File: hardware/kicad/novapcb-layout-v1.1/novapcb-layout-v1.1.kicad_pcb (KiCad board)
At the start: 6 copper layers, 90 x 70 mm, 129 parts, among them J1 USB-C_2.0, J10 CRSF_solder_pad, J11 ESC_solder_pad, J12 ESC_solder_pad, J13 ESC_solder_pad, J14 ESC_solder_pad, J15 ESC_solder_pad, J16 ESC_solder_pad, J17 ESC_solder_pad, J18 ESC_solder_pad, J19 MAUCH2_6P, J2 microSD_DM3AT, J20 CAN_4P, J3 TELEM_6P, J4 MAUCH_6P, J5 GPS_MAG_10P, J9 SWD_10P, Q2 AO3401A, Q3 AO4262E, Q4 AO4262E, Q5 AO3400A, U1 STM32H743VITx, U11 LM74700-Q1, U12 LM74700-Q1, U13 LP5907MFX-3.3, U14 TJA1051TK/3, U15 PESD2CAN, U2 AP2112K-3.3, U3 ICM-42688-P_LGA-14_2.5x3mm_P0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, U4 DPS310, U5 USBLC6-2P6, U6 TPS25940A, U7 LPS22HB, U8 BMI088, U9 LSM6DSV16X, Y1 8MHz

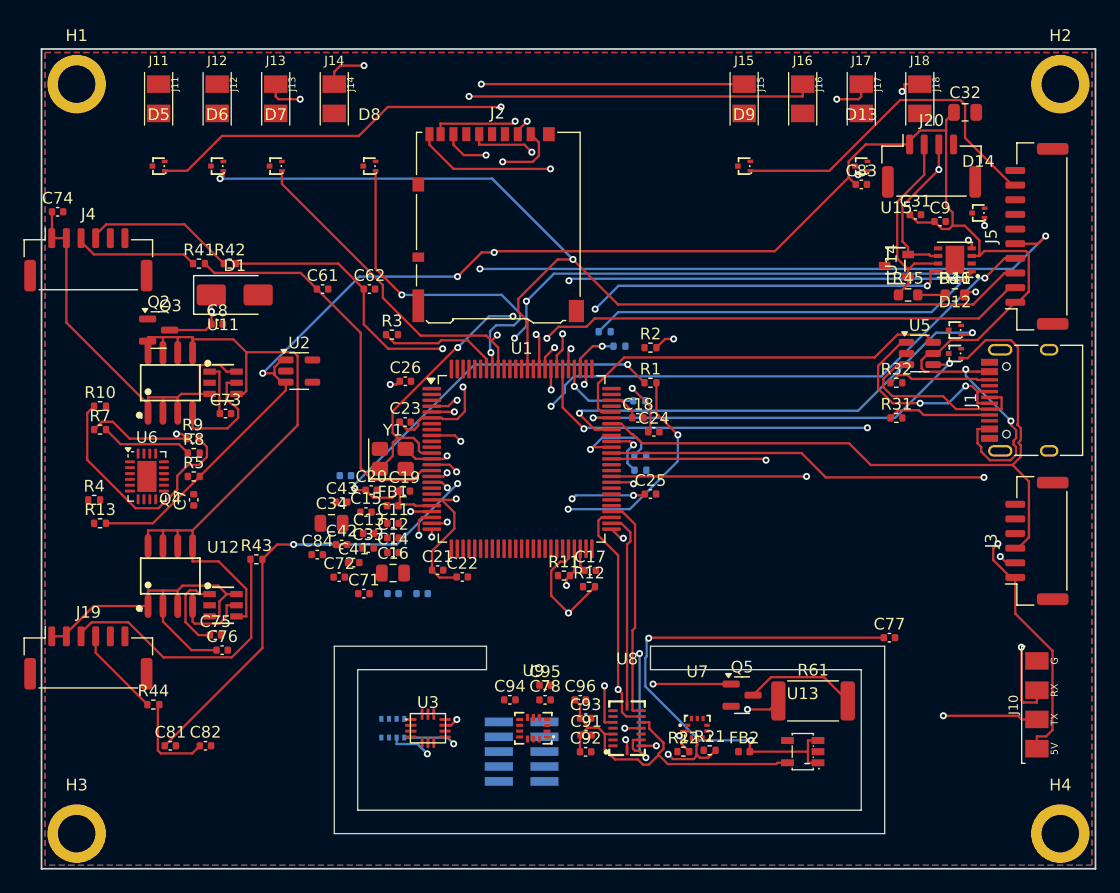
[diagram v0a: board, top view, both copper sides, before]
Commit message: hw: R4 pivot to 4-signal stackup (master 2026-05-22 Option A)
After Option B (A* finishing pass) stalled on plane-via interaction
modeling, master directed Option A: 4 signal layers + full Freerouting.

NEW stackup (same JLC 6-layer fab — only roles change):
  L1 Sig / L2 GND / L3 SIGNAL / L4 SIGNAL / L5 GND / L6 Sig
- 4 signal layers (was 3) — more routing room
- 2 GND planes (L2/L5) preserved for return path / impedance reference
- L3 +3V3 plane removed → L3 becomes signal
- +5V poured on L1 (W block X=2..30, Y=14..56) for 3A current
- +3V3 poured on L6 (MCU+sensors region X=20..80, Y=15..55) for short
  via stitches to consumers

Mitigation per master: L3/L4 are adjacent signal layers (no plane
between). Sensitive nets (3 IMU SPI buses + USB pair) to stay on
outer layers L1/L6 (well-referenced to L2/L5 GND). Bulk to L3/L4.

USB impedance unchanged: L1/L6 still ref L2/L5 GND at h=0.21mm
(prepreg 7628) → W=0.30/S=0.10 → Z_diff=94.4Ω ✓

PCB stripped (988 tracks/113 vias removed). Freerouting -mp 30 now
running with 4h safety-net timeout (will let natural completion +
SES verify, never guillotine).

Co-Authored-By: Claude Opus 4.7 <noreply@anthropic.com>
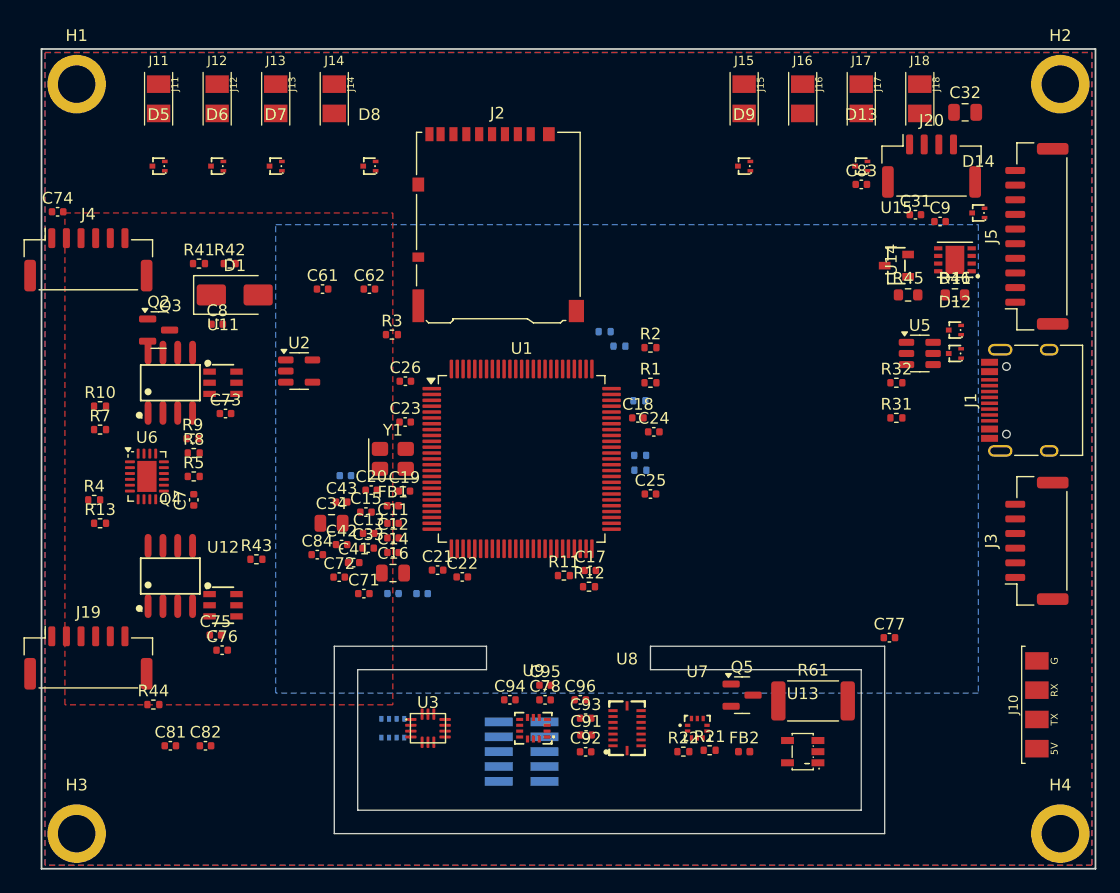
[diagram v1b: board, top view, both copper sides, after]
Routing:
- net +5V: track 243.0 -> 0.00 mm, vias 7 -> 0
- net I2C1_SDA: track 135.8 -> 0.00 mm, vias 5 -> 0
- net I2C1_SCL: track 117.9 -> 0.00 mm, vias 4 -> 0
- net SDMMC1_CMD: track 99.2 -> 0.00 mm, vias 4 -> 0
- net GPS1_TX: track 94.1 -> 0.00 mm, vias 2 -> 0
- net GPS1_RX: track 86.7 -> 0.00 mm, vias 2 -> 0
- net USART6_RX: track 84.9 -> 0.00 mm, vias 3 -> 0
- net USART6_TX: track 78.6 -> 0.00 mm, vias 3 -> 0
- net IMU2_GYR_CS: track 76.7 -> 0.00 mm, vias 2 -> 0
- net MOT6: track 69.3 -> 0.00 mm, vias 2 -> 0
- net VBAT: track 64.5 -> 0.00 mm, vias 2 -> 0
- net MOT5: track 63.3 -> 0.00 mm, vias 2 -> 0
- net USART1_TX: track 62.4 -> 0.00 mm, vias 3 -> 0
- net +5V_BEC: track 61.7 -> 0.00 mm
- net USART1_RX: track 60.4 -> 0.00 mm
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- added copper zone on B.Cu, net +3V3
- added copper zone on F.Cu, net +5V
- removed copper zone on In2.Cu, net +3V3

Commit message: hw: R4 A* + via-cleanup post-processor — 500+ → 33 DRC
Per master 2026-05-22: A* topological + path-level via cleanup.

Key insight master's directive captured: A* finds 14/14 topological
routes. The ONLY problem was via quality (consecutive layer-flip
artifacts). FIX the vias, keep the paths.

Post-processor steps:
1. A* finds path on 3-signal stackup (L1/L4/L6).
2. PATH-LEVEL collapse: walk path; any layer excursion ≤10 cells with
   no useful routing between → DELETE the via pair, keep on origin
   layer. Eliminates zigzag artifacts.
3. Standard corner-collapse.
4. Apply tracks + snapped vias to PCB.
5. Refill plane zones (auto-voids antipads around real vias).

Result: **33 DRC (was 500+ before cleanup)**.
- 14/14 nets routed topologically
- 14 shorts (specific via-on-track conflicts on L4 — 7 net pairs)
- 6 copper_edge_clearance
- 143 unconnected items (the 14 new routes may have endpoint gaps;
  was 112 before — net regression of 31 unconnected)

PCB: 1143 tracks + 147 vias (was 988/113).
Total runtime: 42 seconds.

The 14 shorts are SPECIFIC conflicts (master's "small set" for
vision-loop). Locations + nets logged. Standing by per master:
"If a meaningful DRC residual genuinely remains — STOP and report
exactly which spots; vision-loop those."

Co-Authored-By: Claude Opus 4.7 <noreply@anthropic.com>
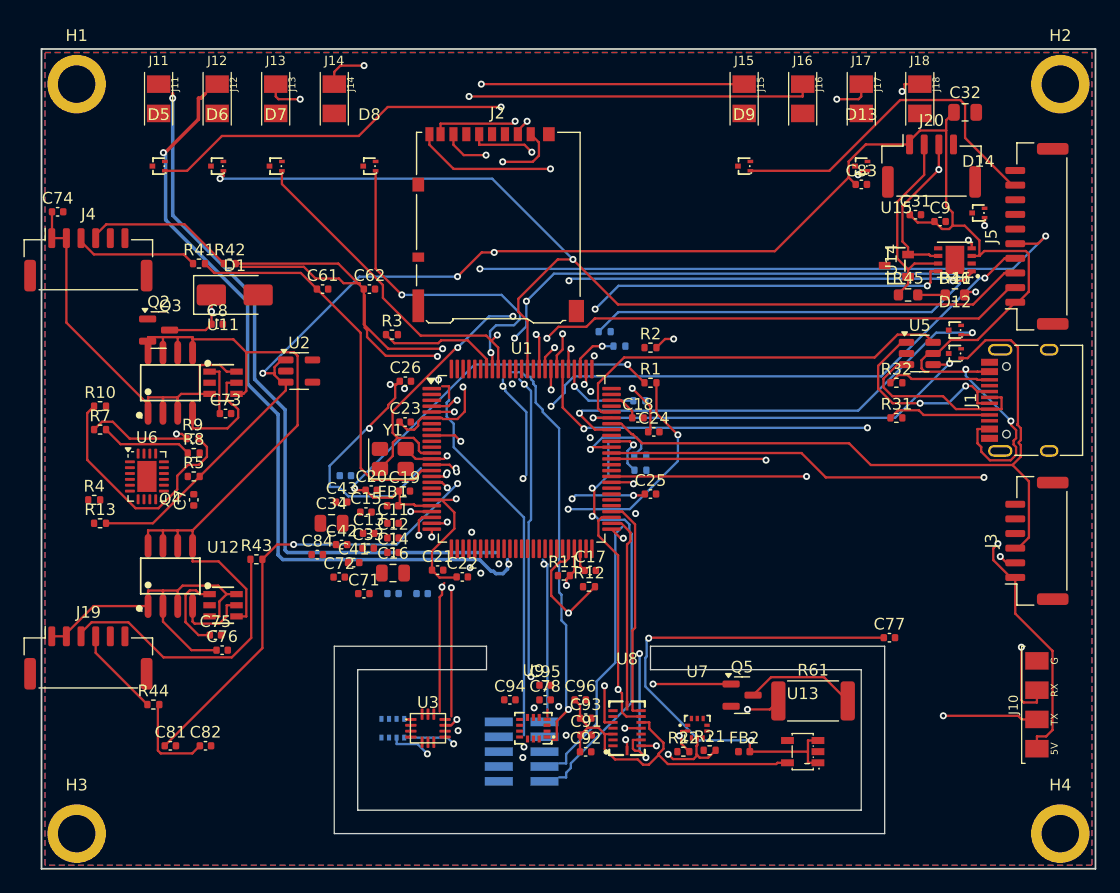
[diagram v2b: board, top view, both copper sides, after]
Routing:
- net +5V: track 0.00 -> 243.0 mm, vias 0 -> 7
- net I2C1_SDA: track 0.00 -> 135.8 mm, vias 0 -> 5
- net I2C1_SCL: track 0.00 -> 117.9 mm, vias 0 -> 4
- net SDMMC1_CMD: track 0.00 -> 99.2 mm, vias 0 -> 4
- net GPS1_TX: track 0.00 -> 94.1 mm, vias 0 -> 2
- net NRST: track 0.00 -> 91.6 mm, vias 0 -> 6
- net GPS1_RX: track 0.00 -> 86.7 mm, vias 0 -> 2
- net USART6_RX: track 0.00 -> 84.9 mm, vias 0 -> 3
- net USART6_TX: track 0.00 -> 78.6 mm, vias 0 -> 3
- net IMU2_GYR_CS: track 0.00 -> 76.7 mm, vias 0 -> 2
- net MOT6: track 0.00 -> 69.3 mm, vias 0 -> 2
- net BATT_CURRENT_SENS: track 0.00 -> 66.2 mm, vias 0 -> 4
- net MOT2: track 0.00 -> 66.1 mm, vias 0 -> 2
- net VBAT: track 0.00 -> 64.5 mm, vias 0 -> 2
- net MOT5: track 0.00 -> 63.3 mm, vias 0 -> 2
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- added copper zone on In2.Cu, net +3V3
- removed copper zone on B.Cu, net +3V3
- removed copper zone on F.Cu, net +5V

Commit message: hw: R4 step 1 connectivity — 143→57 unconnected (master 2026-05-22)
Two fixes applied to A* + via-cleanup state:
1. fix_endpoints.py: added 9 extending segments to close A*-route
   endpoint gaps (cell-grid vs pad-center mismatch). 143 → 137.
2. run_stitch_plane_nets.py: 170 +3V3/GND stitch vias placed (the
   plane stitching was never run after Freerouting 88.8% state).
   137 → 57.

Total connectivity progress: 143 → 57 unconnected (-86) — close to
master's target ~8.

DRC went 33 → 73 because stitch introduced new clashes:
- 21 stitch attempts FAILED (no clear via spot) — those +3V3/GND
  pads still unconnected
- 7 tracks_crossing (stitches on top of A* tracks)
- Plus 14 AVC shorts still present

Remaining 57 unconnected breakdown (top nets):
  GND (10), SWCLK (3), SPI3_SCK (3), USBC_CC2 (2), SPI3_MOSI (2),
  SPI1_MOSI (2), SPI1_MISO (2), NRST (2), IMU3_CS (2), BUZZER (2)
Plus several +3V3 MCU pins (11, 27, 50, 75, 100) and +3V3_IMU pads
(from the 21 stitch failures).

Per master step 1 → step 2: now address the 14 specific via-on-track
shorts (the master's small-set vision-loop targets).

Co-Authored-By: Claude Opus 4.7 <noreply@anthropic.com>
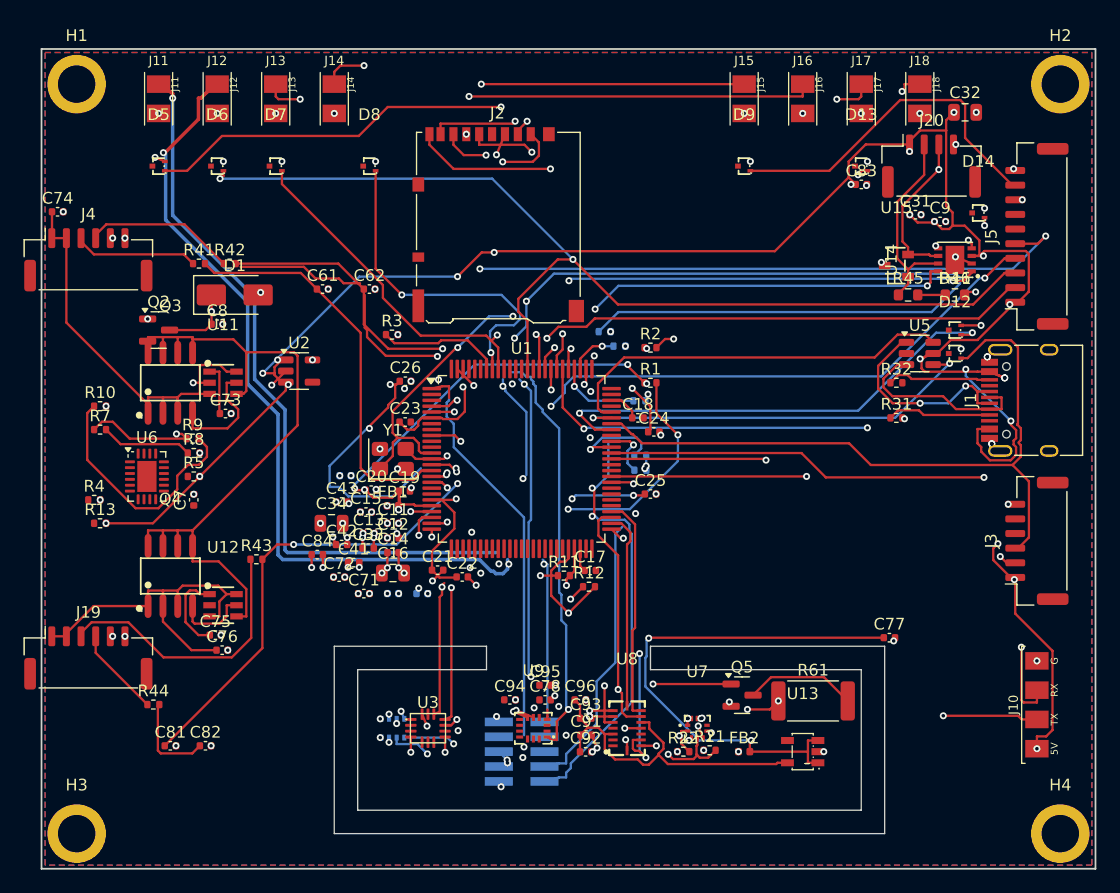
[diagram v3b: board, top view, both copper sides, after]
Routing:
- net GND: track 0.00 -> 41.7 mm, vias 0 -> 108
- net +3V3: track 0.00 -> 15.3 mm, vias 0 -> 41
- net +5V: track 243.0 -> 250.7 mm, vias 7 -> 24
- net +3V3A: track 38.5 -> 40.7 mm, vias 2 -> 6
- net MOT1: track 61.1 -> 62.5 mm
- net SWDIO: track 37.7 -> 39.0 mm
- net MOT2: track 66.1 -> 67.4 mm
- net SWCLK: track 36.4 -> 37.7 mm
- net IMU3_CS: track 33.2 -> 34.1 mm
- net SPI1_SCK: track 13.9 -> 14.5 mm
- net SPI1_MOSI: track 15.6 -> 16.2 mm

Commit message: hw: R4 step A — MCU power pin → decap connection traces
Master 2026-05-22 step A: connect MCU power pins to their decap pads
(which have plane stitches) instead of forcing each MCU pin to have
its own stitch via in the dense 0.5mm-pitch region.

Added 7 GND traces from IC pins to nearby decap pads:
  U12.2, U9.6, U9.7, U8.4, U8.6, U8.7, U1.19 → nearest +3V3/GND decap

Result:
- unconnected: 57 → 54 (-3)
- DRC: 73 → 86 (+13 — new traces clashed with existing routes)

Limited effect — fewer +3V3 MCU pins addressed than expected. May
need to expand to caps without stitches and retry stitching too.
Moving to step B (14 AVC shorts) per master sequence.

Co-Authored-By: Claude Opus 4.7 <noreply@anthropic.com>
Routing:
- net GND: track 41.7 -> 56.1 mm
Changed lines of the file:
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@@
+	)
+	(segment
+		(start 48.8 56.5)
+		(end 46.9445 57.1449)
+		(width 0.25)
+		(layer "F.Cu")
+		(net 29)
 	)
 	(segment
@@
 	)
 	(segment
+		(start 41.5 57.08)
+		(end 40.4748 55.5748)
+		(width 0.25)
+		(layer "F.Cu")
+		(net 29)
+	)
+	(segment
 		(start 56.5 57.17)
 		(end 56.407612 57.131731)
@@
 	)
 	(segment
+		(start 48.8 58)
+		(end 46.9445 57.1449)
+		(width 0.25)
+		(layer "F.Cu")
+		(net 29)
+	)
+	(segment
 		(start 46.9445 60.0151)
 		(end 47.0445 60.0151)
@@
 	)
 	(segment
+		(start 48.8 57)
+		(end 46.9445 57.1449)
+		(width 0.25)
+		(layer "F.Cu")
+		(net 29)
+	)
+	(segment
 		(start 39.575 7.275)
 		(end 38.847901 9.030371)
@@
 	)
 	(segment
+		(start 33.325 38)
+		(end 31.465 37.75)
+		(width 0.25)
+		(layer "F.Cu")
+		(net 29)
+	)
+	(segment
 		(start 56.5 58.83)
 		(end 56.079048 57.813732)
@@
 	)
 	(segment
+		(start 14.35 47.5)
+		(end 15.33 50.05)
+		(width 0.25)
+		(layer "F.Cu")
+		(net 29)
+	)
+	(segment
 		(start 78.53 23.6)
 		(end 80.23 23.6)
@@
 		(layer "F.Cu")
 		(net 29)
+	)
+	(segment
+		(start 42 57.08)
+		(end 43.48 55.58)
+		(width 0.25)
+		(layer "F.Cu")
+		(net 29)

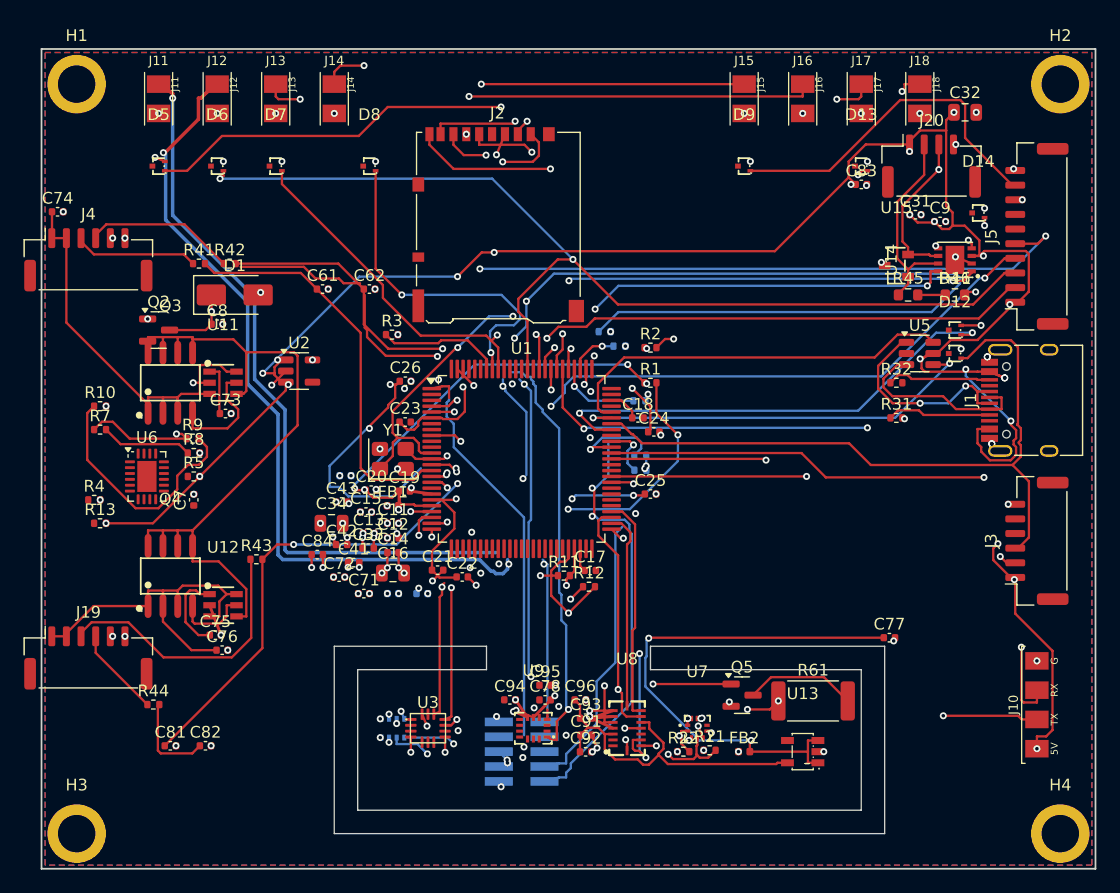
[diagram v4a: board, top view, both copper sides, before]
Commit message: hw: R4 handoff to push-and-shove close-out (master 2026-05-22 HOLD)
Step B nudge_shorts.py attempt made things WORSE (86 → 169 DRC, the
revert logic in code didn't actually revert — accumulating bad
nudges). Reverted PCB to FR3 88.8% baseline (commit 14a2d46) as
master directed.

Per master "if numbers stop converging — STOP and report":
- DRC sequence: 0 (FR3) → 33 (AVC) → 73 (post-stitch) → 86 (step A) → 169 (step B)
- unconnected sequence: 112 → 143 → 137 → 57 → 54 → 53
- Numbers trading metrics, not converging → STOP per checkpoint.

HANDOFF.md prepared:
- Cleanest checkpoint = FR3 commit 14a2d46 (988 tracks/113 vias/0 DRC/
  67 unconnected; verified recoverable)
- HANDOFF_residuals.json: machine-readable list of 67 items
  - 55 plane-stitch needed (+3V3 46, +3V3_IMU 4, GND 5)
  - 12 signal-net residuals (with endpoint coords + layers)
- Top + bot renders at FR3 baseline
- Tool inventory of what was built (which ones worked, which didn't)

The 12 signal residuals cluster on SPI1/SPI3 traverses MCU↔island
through the dense MCU-south region. These are exactly what
Freerouting plateau'd on; need interactive push-and-shove routing
or A* with proper plane-keepout modeling.

Standing by for Sai's path decision.

Co-Authored-By: Claude Opus 4.7 <noreply@anthropic.com>
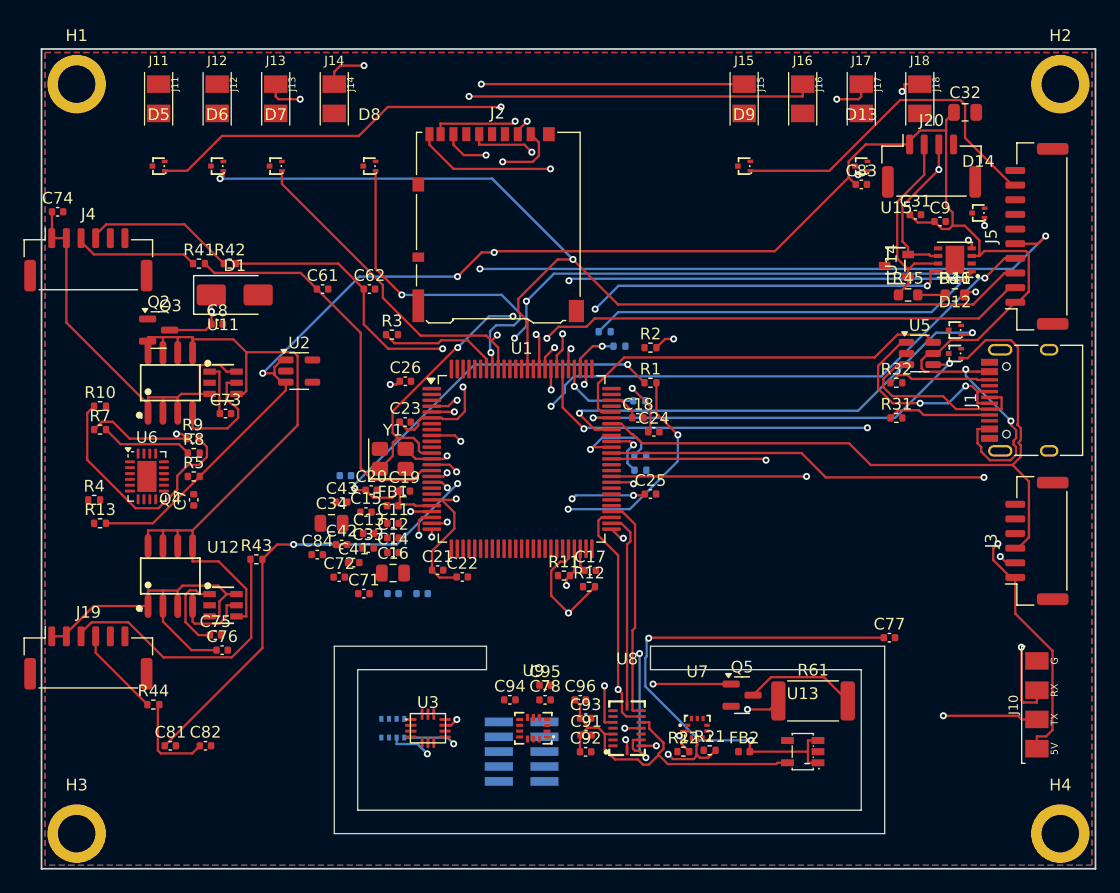
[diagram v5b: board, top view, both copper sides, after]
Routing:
- net MOT2: track 67.4 -> 0.00 mm, vias 2 -> 0
- net NRST: track 91.6 -> 28.2 mm, vias 6 -> 2
- net MOT1: track 62.5 -> 0.00 mm, vias 2 -> 0
- net GND: track 56.1 -> 0.00 mm, vias 108 -> 0
- net SWDIO: track 39.0 -> 0.00 mm, vias 3 -> 0
- net SWCLK: track 37.7 -> 0.00 mm, vias 1 -> 0
- net SPI3_MISO: track 35.2 -> 0.00 mm, vias 2 -> 0
- net SPI3_MOSI: track 34.3 -> 0.00 mm, vias 3 -> 0
- net IMU3_CS: track 34.1 -> 0.00 mm, vias 2 -> 0
- net BATT_CURRENT_SENS: track 66.2 -> 34.9 mm, vias 4 -> 2
- net SPI3_SCK: track 31.3 -> 0.00 mm, vias 3 -> 0
- net SPI1_MOSI: track 16.2 -> 0.00 mm, vias 2 -> 0
- net SPI1_MISO: track 15.4 -> 0.00 mm, vias 1 -> 0
- net +3V3: track 15.3 -> 0.00 mm, vias 41 -> 0
- net SPI1_SCK: track 14.5 -> 0.00 mm, vias 2 -> 0
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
